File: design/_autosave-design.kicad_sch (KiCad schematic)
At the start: 29 parts, among them J1 Conn_01x03_Pin, J2 Conn_01x02_Pin, J3 Conn_01x02_Pin, U1 MC7912, U2 L7812, U3 OPA209AID, U4 TL082

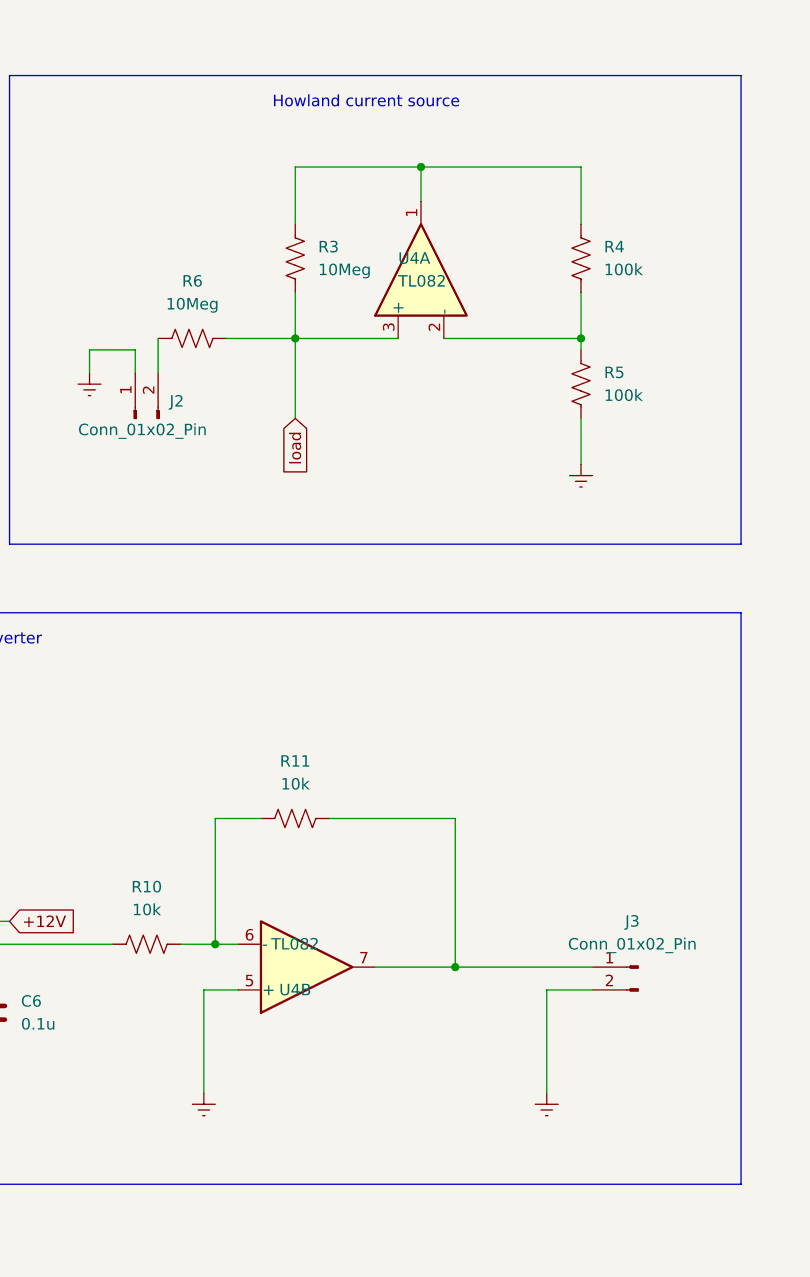
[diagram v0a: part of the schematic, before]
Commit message: Cambios muy importantes en PCB y schematic de KiCad
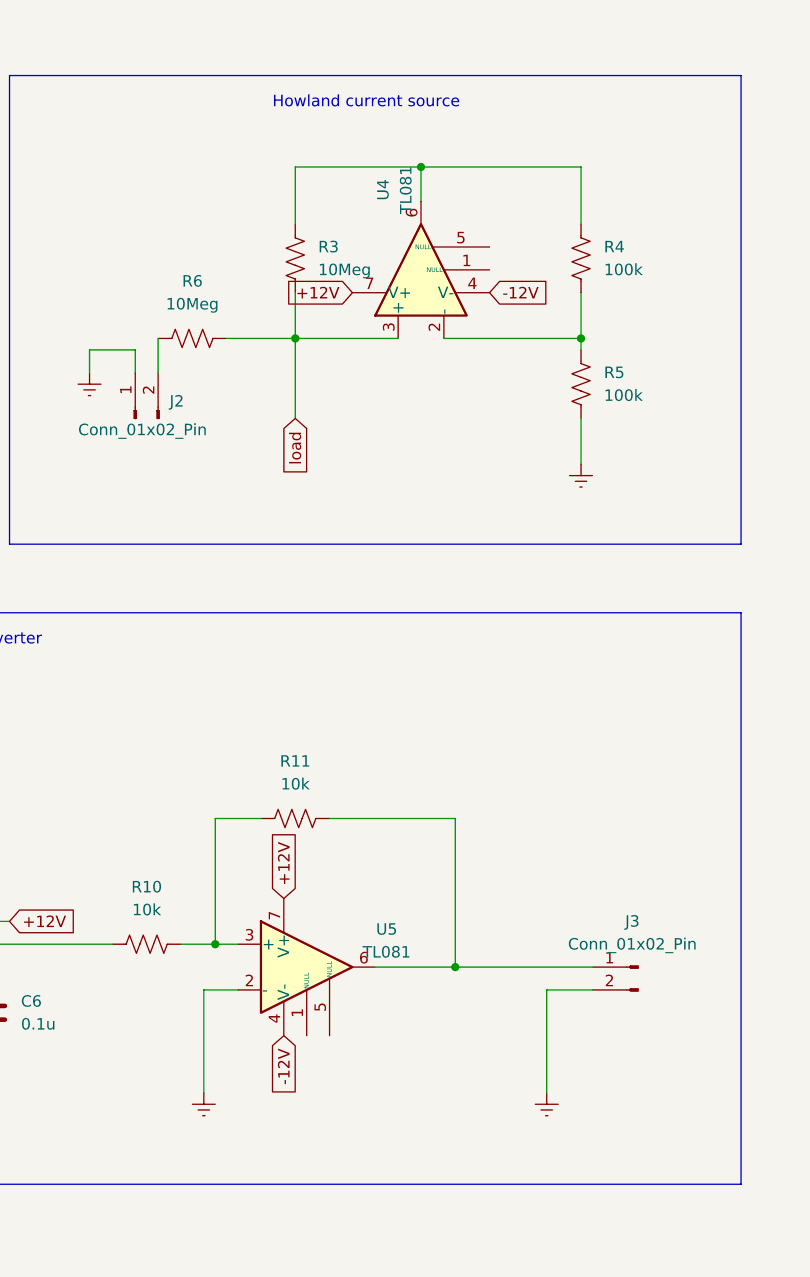
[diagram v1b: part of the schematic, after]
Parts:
- removed U4: TL082, Package_DIP:DIP-8_W7.62mm_LongPads, symbol Amplifier_Operational:TL082
- added U4, U5: TL081, Package_DIP:DIP-8_W7.62mm_LongPads, symbol Amplifier_Operational:TL081
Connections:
- net +12V: now also U4.7 (V+), U5.7 (V+)
- net -12V: now also U4.4 (V-), U5.4 (V-)
- net Earth: now also U5.2 (-)
- net load: now also U4.3 (+)
- net at J3.1 (Pin_1), R11.1: now also U5.6
- net at R10.1, R11.2: now also U5.3 (+)
- net at R4.1, R5.2: now also U4.2 (-)
- net at R3.2, R4.2: now also U4.6
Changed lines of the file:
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@@
+    )
+  )
+  (global_label "-12V" (shape input) (at 214.63 46.99 0) (fields_autoplaced)
+    (effects (font (size 1.27 1.27)) (justify left))
+    (property "Intersheetrefs" "${INTERSHEET_REFS}" (at 222.6952 46.99 0)
+      (effects (font (size 1.27 1.27)) (justify left) hide)
     )
   )
@@
     )
   )
+  (global_label "-12V" (shape input) (at 191.77 129.54 270) (fields_autoplaced)
+    (effects (font (size 1.27 1.27)) (justify right))
+    (property "Intersheetrefs" "${INTERSHEET_REFS}" (at 191.77 137.6052 90)
+      (effects (font (size 1.27 1.27)) (justify right) hide)
+    )
+  )
+  (global_label "+12V" (shape input) (at 199.39 46.99 180) (fields_autoplaced)
+    (effects (font (size 1.27 1.27)) (justify right))
+    (property "Intersheetrefs" "${INTERSHEET_REFS}" (at 191.3248 46.99 0)
+      (effects (font (size 1.27 1.27)) (justify right) hide)
+    )
+  )
   (global_label "load" (shape input) (at 80.01 111.76 180) (fields_autoplaced)
     (effects (font (size 1.27 1.27)) (justify right))
@@
     )
   )
+  (global_label "+12V" (shape input) (at 191.77 114.3 90) (fields_autoplaced)
+    (effects (font (size 1.27 1.27)) (justify left))
+    (property "Intersheetrefs" "${INTERSHEET_REFS}" (at 191.77 106.2348 90)
+      (effects (font (size 1.27 1.27)) (justify left) hide)
+    )
+  )
   (global_label "load" (shape input) (at 193.04 60.96 270) (fields_autoplaced)
     (effects (font (size 1.27 1.27)) (justify right))
@@
     )
   )
-  (symbol (lib_id "Amplifier_Operational:TL082") (at 207.01 44.45 90) (unit 1)
-    (in_bom yes) (on_board yes) (dnp no)
-    (property "Reference" "U4" (at 204.47 43.18 90)
-      (effects (font (size 1.27 1.27)) (justify right))
-    )
-    (property "Value" "TL082" (at 204.47 45.72 90)
-      (effects (font (size 1.27 1.27)) (justify right))
-    )
-    (property "Footprint" "Package_DIP:DIP-8_W7.62mm_LongPads" (at 207.01 44.45 0)
-      (effects (font (size 1.27 1.27)) hide)
-    )
-    (property "Datasheet" "http://www.ti.com/lit/ds/symlink/tl081.pdf" (at 207.01 44.45 0)
+  (symbol (lib_id "Amplifier_Operational:TL081") (at 194.31 121.92 0) (unit 1)
+    (in_bom yes) (on_board yes) (dnp no) (fields_autoplaced)
+    (property "Reference" "U5" (at 203.2 117.7291 0)
+      (effects (font (size 1.27 1.27)))
+    )
+    (property "Value" "TL081" (at 203.2 120.2691 0)
+      (effects (font (size 1.27 1.27)))
+    )
+    (property "Footprint" "Package_DIP:DIP-8_W7.62mm_LongPads" (at 195.58 120.65 0)
+      (effects (font (size 1.27 1.27)) hide)
+    )
+    (property "Datasheet" "http://www.ti.com/lit/ds/symlink/tl081.pdf" (at 198.12 118.11 0)
       (effects (font (size 1.27 1.27)) hide)
     )
@@
     (pin "2")
     (pin "3")
+    (pin "4")
     (pin "5")
     (pin "6")
     (pin "7")
-    (pin "4")
     (pin "8")
     (instances
       (project "design"
         (path "/a520f27b-3eb4-44e7-9faf-250bc52b55ee"
-          (reference "U4") (unit 1)
+          (reference "U5") (unit 1)
         )
       )
@@
     )
   )
-  (symbol (lib_id "Amplifier_Operational:TL082") (at 194.31 121.92 0) (mirror x) (unit 2)
-    (in_bom yes) (on_board yes) (dnp no)
-    (property "Reference" "U4" (at 193.04 124.46 0)
-      (effects (font (size 1.27 1.27)))
-    )
-    (property "Value" "TL082" (at 193.04 119.38 0)
-      (effects (font (size 1.27 1.27)))
-    )
-    (property "Footprint" "Package_DIP:DIP-8_W7.62mm_LongPads" (at 194.31 121.92 0)
-      (effects (font (size 1.27 1.27)) hide)
-    )
-    (property "Datasheet" "http://www.ti.com/lit/ds/symlink/tl081.pdf" (at 194.31 121.92 0)
+  (symbol (lib_id "Amplifier_Operational:TL081") (at 207.01 44.45 90) (unit 1)
+    (in_bom yes) (on_board yes) (dnp no) (fields_autoplaced)
+    (property "Reference" "U4" (at 202.8191 35.56 0)
+      (effects (font (size 1.27 1.27)))
+    )
+    (property "Value" "TL081" (at 205.3591 35.56 0)
+      (effects (font (size 1.27 1.27)))
+    )
+    (property "Footprint" "Package_DIP:DIP-8_W7.62mm_LongPads" (at 205.74 43.18 0)
+      (effects (font (size 1.27 1.27)) hide)
+    )
+    (property "Datasheet" "http://www.ti.com/lit/ds/symlink/tl081.pdf" (at 203.2 40.64 0)
       (effects (font (size 1.27 1.27)) hide)
     )
@@
     (pin "2")
     (pin "3")
+    (pin "4")
     (pin "5")
     (pin "6")
     (pin "7")
-    (pin "4")
     (pin "8")
     (instances
       (project "design"
         (path "/a520f27b-3eb4-44e7-9faf-250bc52b55ee"
-          (reference "U4") (unit 2)
-        )
-      )
+          (reference "U4") (unit 1)
+        )
+      )
